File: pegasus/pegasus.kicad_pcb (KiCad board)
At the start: 2 copper layers, 50.8 x 126.4 mm, 10 parts, among them IC1 RFD900, IC2 Adafruit_MPL3115A2, IC3 Adafruit-BNO055-PCB, IC4 L70B-M39, IC5 L7805ACV, J1 Conn_01x02_Female, J2 Conn_01x02_Female, U1 Teensy4.1, U2 CON-SMA-EDGE-S, U3 CON-SMA-EDGE-S

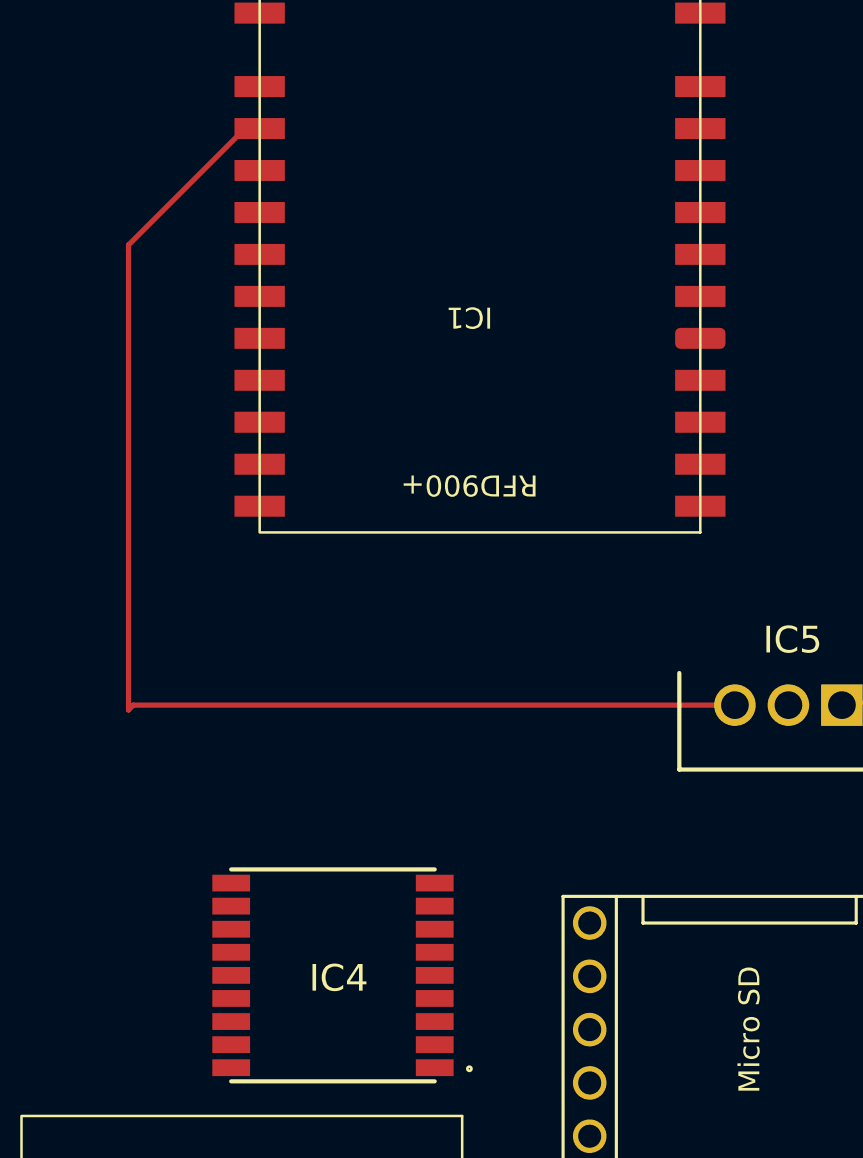
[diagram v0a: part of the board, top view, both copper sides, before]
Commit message: fixed UART wiring for gps and modem
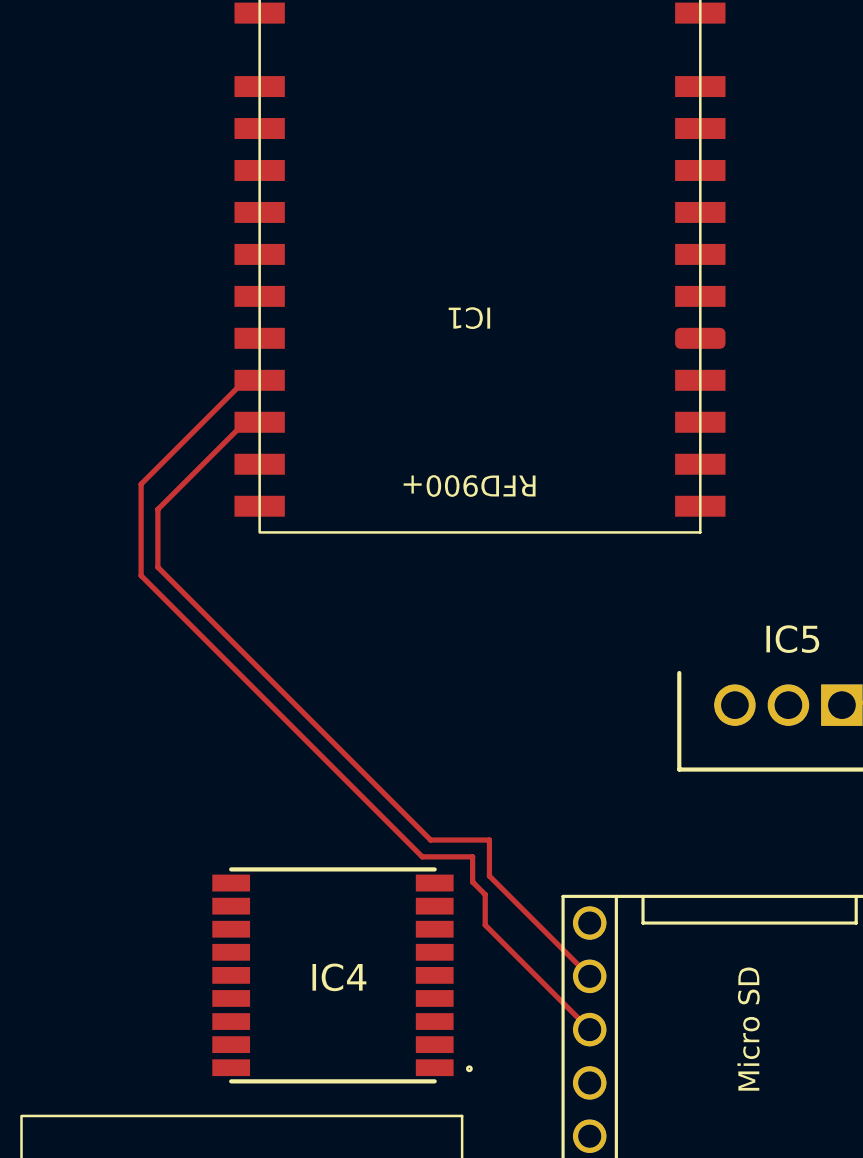
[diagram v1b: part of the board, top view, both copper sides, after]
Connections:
- net Net-(IC4-Pad2) renamed RX1
- net Net-(IC4-Pad3) renamed TX1
- U1 pad 26: Net-(IC1-Pad25) -> Net-(IC1-Pad26)
- U1 pad 27: Net-(IC1-Pad26) -> Net-(IC1-Pad25)
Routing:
- net /+5V: track 59.7 -> 0.70 mm
- net Net-(IC1-Pad25): track 0.00 -> 44.0 mm
- net Net-(IC1-Pad26): track 0.00 -> 39.0 mm

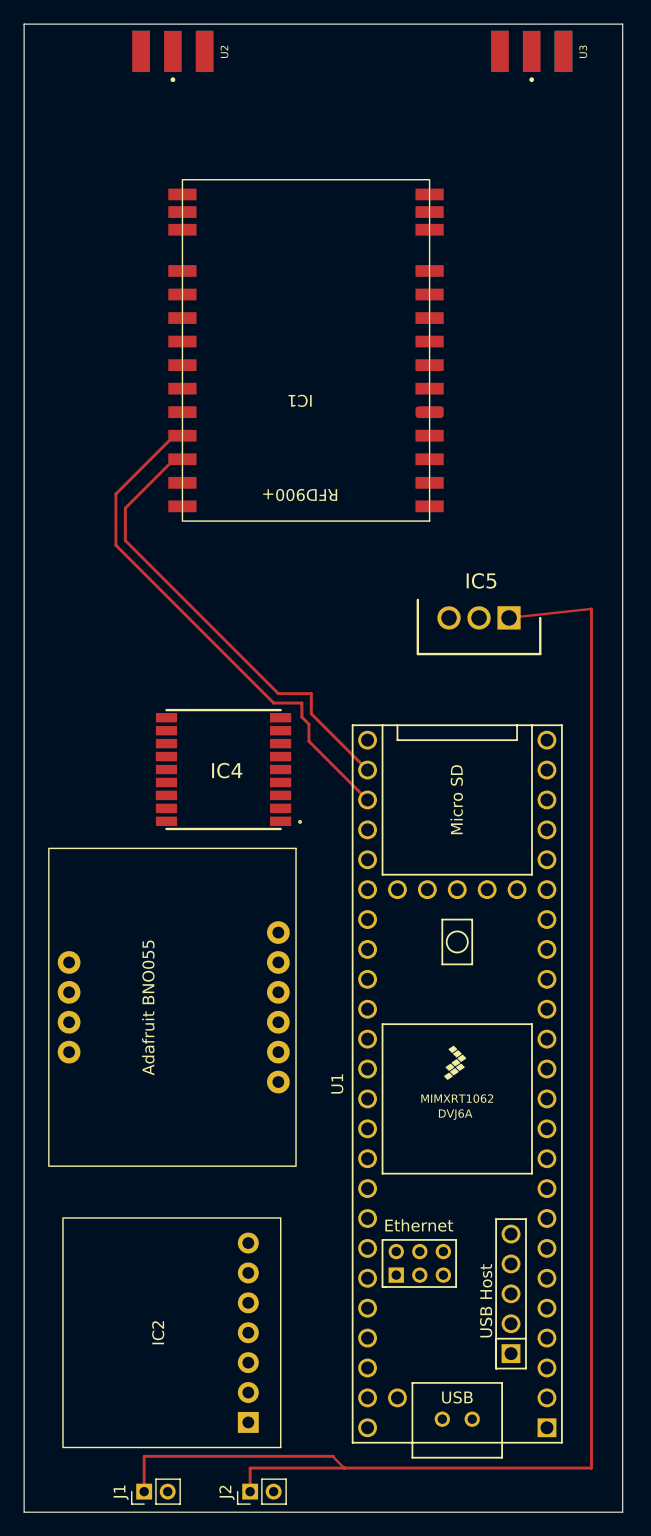
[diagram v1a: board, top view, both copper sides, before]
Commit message: finalized board dimensions (50x120mm) and component positioning. completed draft of traces
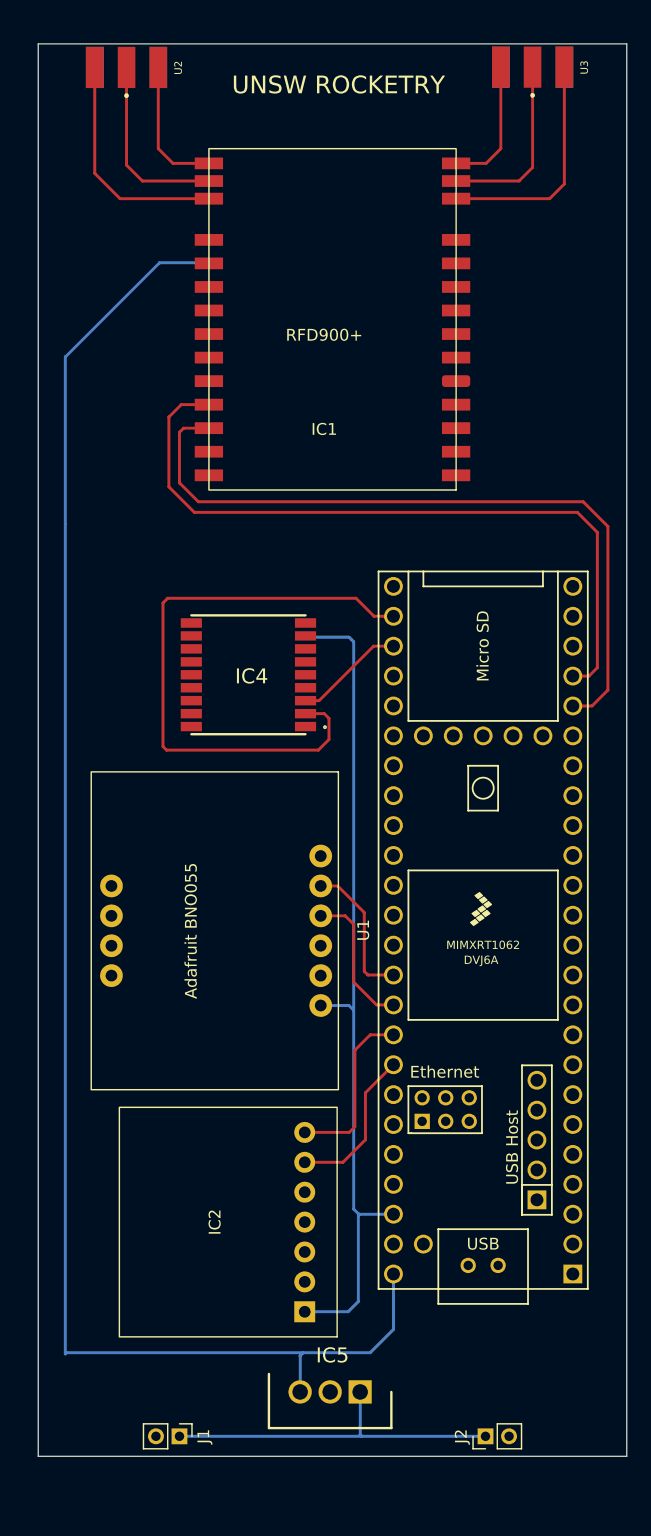
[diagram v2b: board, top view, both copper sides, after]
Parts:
- moved IC5 67.0 mm to (107.3, 154.5)
- moved J2 20.5 mm to (118.0, 158.3)
- moved U1 13.2 mm to (117.8, 115.3)
- moved IC2 10.6 mm to (100.1, 140.1)
- moved IC4 8.32 mm to (97.9, 93.6)
- moved IC3 7.43 mm to (104.0, 115.3)
- moved J1 5.58 mm to (92.0, 158.3), turned to -90 degrees
- moved U2 4.17 mm to (87.5, 42.0)
- moved IC1 3.47 mm to (109.5, 66.7)
- moved U3 1.33 mm to (122.0, 42.0)
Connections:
- net Net-(IC2-Pad1) renamed /+3.3V
- net Net-(IC2-Pad6) renamed /SCL
- net Net-(IC2-Pad7) renamed /SDA
- net Net-(IC3-Pad4)_1 renamed /SDA1
- net Net-(IC3-Pad5) renamed /SCL1
- IC1 pad 19: /+5V -> +5V
- IC1 pad 25: Net-(IC1-Pad25) -> TX7
- IC1 pad 26: Net-(IC1-Pad26) -> RX7
- IC4 pad 2: RX1 -> RX8
- IC4 pad 3: TX1 -> TX8
- IC5 pad 3: /+5V -> +5V
- U1 pad 2: TX1 -> unconnected-(U1-Pad2)
- U1 pad 20: unconnected-(U1-Pad20) -> RX7
- U1 pad 21: unconnected-(U1-Pad21) -> TX7
- U1 pad 26: Net-(IC1-Pad26) -> RX8
- U1 pad 27: Net-(IC1-Pad25) -> TX8
- U1 pad 3: RX1 -> unconnected-(U1-Pad3)
- U1 pad 48: 3.7V -> +5V
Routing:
- net +5V: track 0.00 -> 137.9 mm
- net 3.7V: track 123.2 -> 29.8 mm
- net /+3.3V: track 0.00 -> 71.3 mm
- net RX7: track 0.00 -> 62.3 mm
- net TX7: track 0.00 -> 61.6 mm
- net RX8: track 0.00 -> 51.1 mm
- net Net-(IC1-Pad25): track 44.0 -> 0.00 mm
- net Net-(IC1-Pad26): track 39.0 -> 0.00 mm
- net Net-(IC1-Pad12): track 0.00 -> 19.6 mm
- net Net-(IC1-Pad17): track 0.00 -> 19.6 mm
- net Net-(IC1-Pad16): track 0.00 -> 15.9 mm
- net Net-(IC1-Pad13): track 0.00 -> 15.5 mm
- net /SDA: track 0.00 -> 14.8 mm
- net /SCL: track 0.00 -> 13.3 mm
- net /SCL1: track 0.00 -> 12.2 mm
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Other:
- board size 50.8 x 126.4 mm -> 50 x 120 mm
- board text added: "UNSW ROCKETRY"

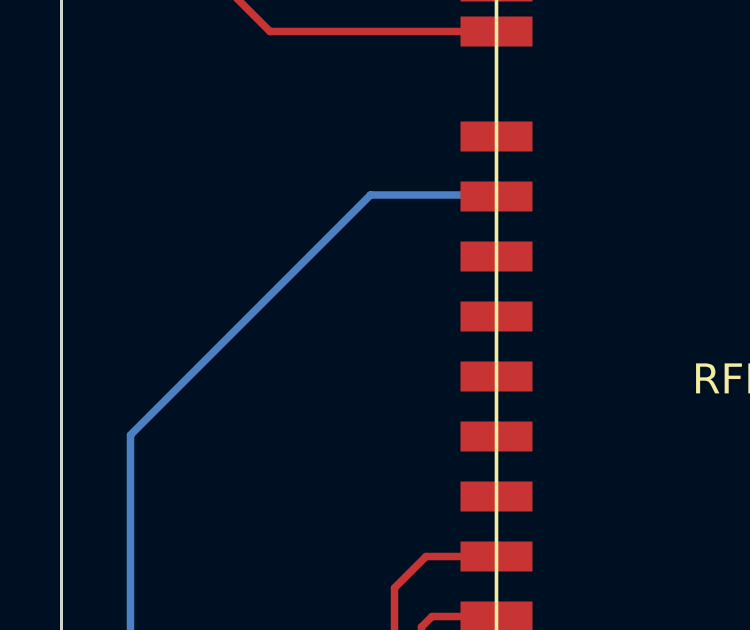
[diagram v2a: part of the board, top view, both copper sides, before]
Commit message: removed a wire
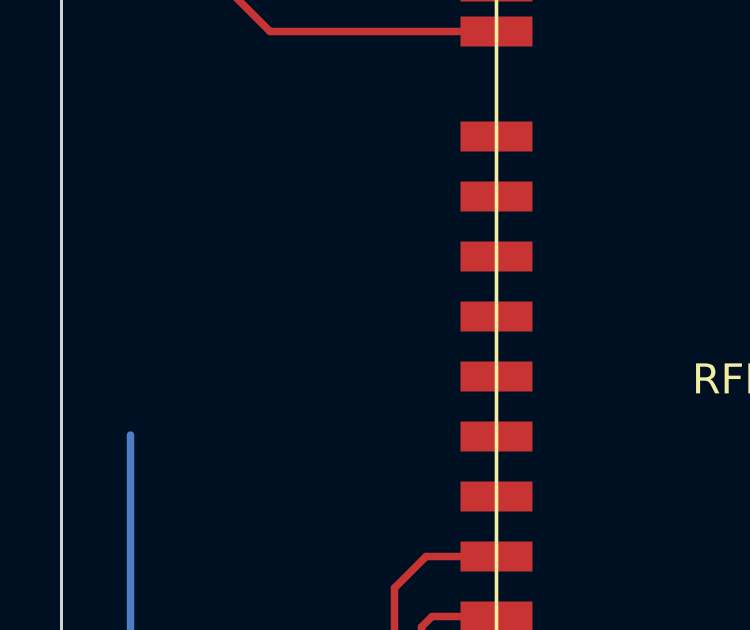
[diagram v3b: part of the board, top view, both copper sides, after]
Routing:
- net +5V: track 137.9 -> 123.3 mm
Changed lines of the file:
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@@
   (segment (start 104 111.54) (end 105.44 111.54) (width 0.25) (layer "F.Cu") (net 107))
   (segment (start 94.5 58.65) (end 93.8 58.65) (width 0.25) (layer "F.Cu") (net 108))
-  (segment (start 82.3 66.6) (end 90.3 58.6) (width 0.25) (layer "B.Cu") (net 108))
   (segment (start 82.3 80.8) (end 82.3 66.6) (width 0.25) (layer "B.Cu") (net 108))
   (segment (start 110.18 149.22) (end 110.18 144.51) (width 0.25) (layer "B.Cu") (net 108))
@@
   (segment (start 82.3 151.3) (end 82.3 80.8) (width 0.25) (layer "B.Cu") (net 108))
   (segment (start 108.2 151.2) (end 110.18 149.22) (width 0.25) (layer "B.Cu") (net 108))
-  (segment (start 90.3 58.6) (end 93.6 58.6) (width 0.25) (layer "B.Cu") (net 108))
   (segment (start 82.4 151.2) (end 82.3 151.3) (width 0.25) (layer "B.Cu") (net 108))
   (segment (start 102.5 151.2) (end 108.2 151.2) (width 0.25) (layer "B.Cu") (net 108))

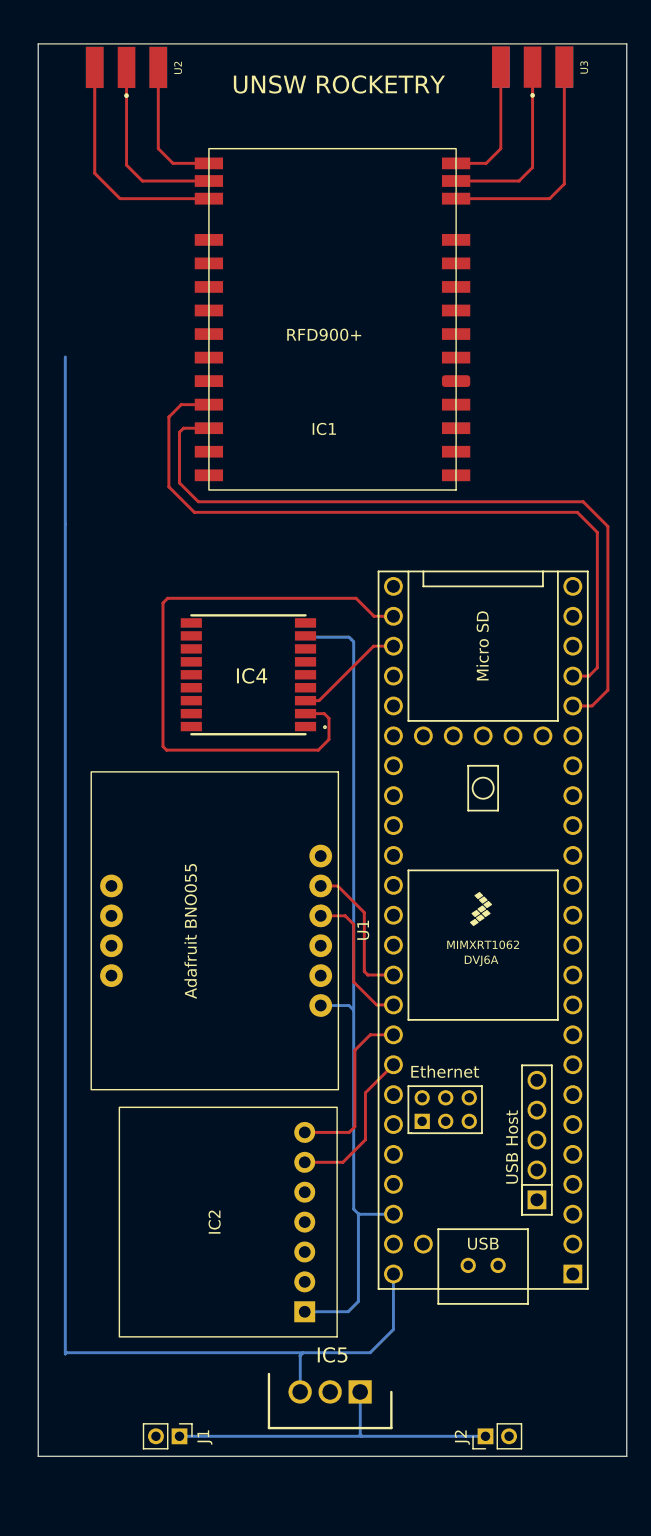
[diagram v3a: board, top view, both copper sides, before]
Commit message: added vias to trace power
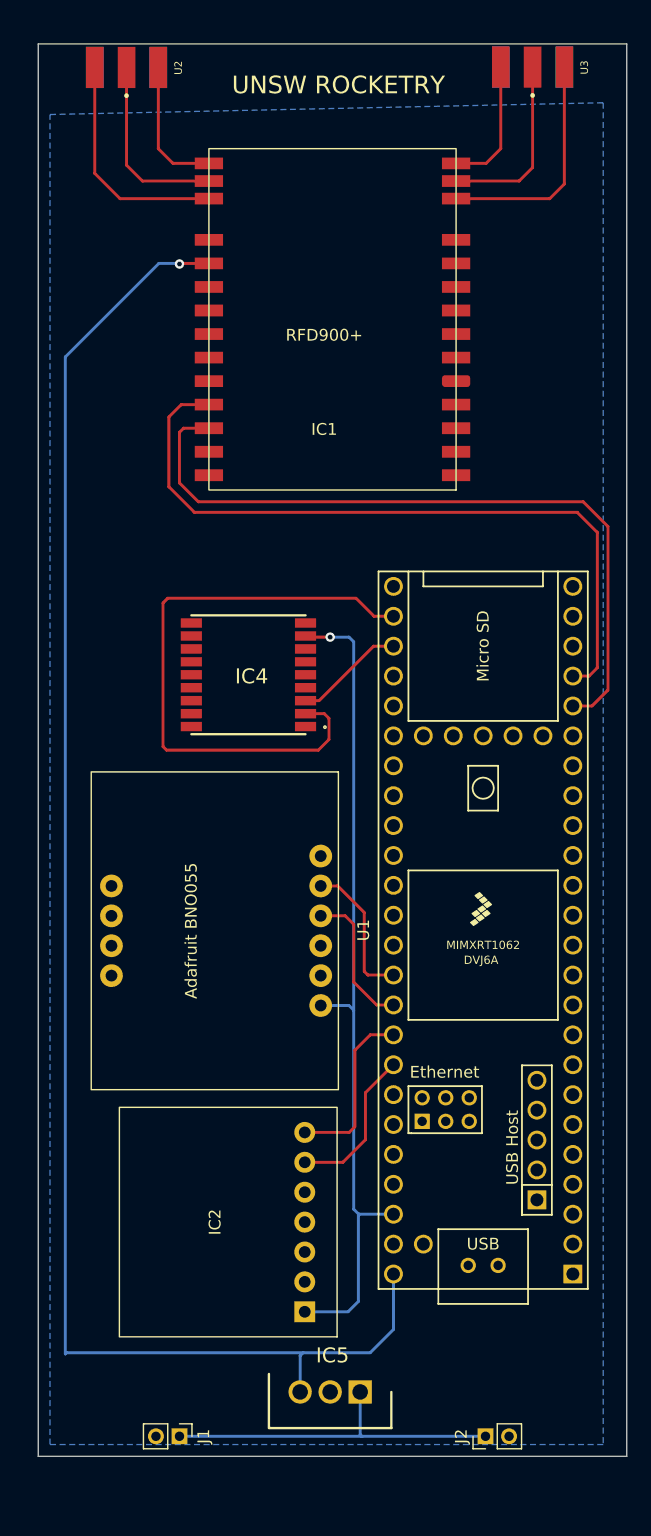
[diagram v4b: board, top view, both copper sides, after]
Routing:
- net +5V: track 123.3 -> 137.1 mm, vias 0 -> 1
- net /+3.3V: track 71.3 -> 71.4 mm, vias 0 -> 1
- added copper zone on B.Cu, net GND
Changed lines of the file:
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@@
   (segment (start 128.4 94.9) (end 128.4 81) (width 0.25) (layer "F.Cu") (net 102))
   (segment (start 92 77.3) (end 92 73) (width 0.25) (layer "F.Cu") (net 102))
+  (segment (start 102.807 90.4) (end 102.707 90.3) (width 0.25) (layer "F.Cu") (net 103))
+  (segment (start 104.8 90.4) (end 102.807 90.4) (width 0.25) (layer "F.Cu") (net 103))
+  (via (at 104.8 90.4) (size 0.8) (drill 0.4) (layers "F.Cu" "B.Cu") (net 103))
   (segment (start 106.32 147.72) (end 102.641 147.72) (width 0.25) (layer "B.Cu") (net 103))
   (segment (start 106.8 139) (end 106.8 122.1) (width 0.25) (layer "B.Cu") (net 103))
   (segment (start 107.25 139.45) (end 106.8 139) (width 0.25) (layer "B.Cu") (net 103))
-  (segment (start 106.4 90.4) (end 102.7 90.4) (width 0.25) (layer "B.Cu") (net 103))
-  (segment (start 106.6 90.6) (end 106.4 90.4) (width 0.25) (layer "B.Cu") (net 103))
+  (segment (start 106.4 90.4) (end 106.8 90.8) (width 0.25) (layer "B.Cu") (net 103))
   (segment (start 107.2 146.84) (end 106.32 147.72) (width 0.25) (layer "B.Cu") (net 103))
   (segment (start 110.18 139.43) (end 107.27 139.43) (width 0.25) (layer "B.Cu") (net 103))
+  (segment (start 106.8 90.8) (end 106.8 122.1) (width 0.25) (layer "B.Cu") (net 103))
   (segment (start 107.27 139.43) (end 107.25 139.45) (width 0.25) (layer "B.Cu") (net 103))
   (segment (start 106.8 122.1) (end 106.4 121.7) (width 0.25) (layer "B.Cu") (net 103))
-  (segment (start 106.8 90.8) (end 106.6 90.6) (width 0.25) (layer "B.Cu") (net 103))
-  (segment (start 106.8 122.1) (end 106.8 90.8) (width 0.25) (layer "B.Cu") (net 103))
+  (segment (start 106.4 90.4) (end 104.8 90.4) (width 0.25) (layer "B.Cu") (net 103))
   (segment (start 107.2 139.5) (end 107.2 146.84) (width 0.25) (layer "B.Cu") (net 103))
   (segment (start 107.25 139.45) (end 107.2 139.5) (width 0.25) (layer "B.Cu") (net 103))
@@
   (segment (start 107.7 113.8) (end 107.7 118.8) (width 0.25) (layer "F.Cu") (net 107))
   (segment (start 104 111.54) (end 105.44 111.54) (width 0.25) (layer "F.Cu") (net 107))
-  (segment (start 94.5 58.65) (end 93.8 58.65) (width 0.25) (layer "F.Cu") (net 108))
-  (segment (start 82.3 80.8) (end 82.3 66.6) (width 0.25) (layer "B.Cu") (net 108))
+  (segment (start 92 58.6) (end 92.05 58.65) (width 0.25) (layer "F.Cu") (net 108))
+  (segment (start 92.05 58.65) (end 94.5 58.65) (width 0.25) (layer "F.Cu") (net 108))
+  (via (at 92 58.7) (size 0.8) (drill 0.4) (layers "F.Cu" "B.Cu") (net 108))
+  (segment (start 102.5 151.2) (end 82.4 151.2) (width 0.25) (layer "B.Cu") (net 108))
   (segment (start 110.18 149.22) (end 110.18 144.51) (width 0.25) (layer "B.Cu") (net 108))
+  (segment (start 91.95 58.65) (end 92 58.7) (width 0.25) (layer "B.Cu") (net 108))
   (segment (start 102.25 151.45) (end 102.5 151.2) (width 0.25) (layer "B.Cu") (net 108))
+  (segment (start 82.3 151.3) (end 82.3 66.6) (width 0.25) (layer "B.Cu") (net 108))
+  (segment (start 90.25 58.65) (end 91.95 58.65) (width 0.25) (layer "B.Cu") (net 108))
   (segment (start 102.25 154.53) (end 102.25 151.45) (width 0.25) (layer "B.Cu") (net 108))
-  (segment (start 93.6 58.6) (end 94.6 58.6) (width 0.25) (layer "B.Cu") (net 108))
-  (segment (start 102.5 151.2) (end 82.4 151.2) (width 0.25) (layer "B.Cu") (net 108))
-  (segment (start 82.3 151.3) (end 82.3 80.8) (width 0.25) (layer "B.Cu") (net 108))
   (segment (start 108.2 151.2) (end 110.18 149.22) (width 0.25) (layer "B.Cu") (net 108))
   (segment (start 82.4 151.2) (end 82.3 151.3) (width 0.25) (layer "B.Cu") (net 108))
   (segment (start 102.5 151.2) (end 108.2 151.2) (width 0.25) (layer "B.Cu") (net 108))
+  (segment (start 82.3 66.6) (end 90.25 58.65) (width 0.25) (layer "B.Cu") (net 108))
+  (zone (net 2) (net_name "GND") (layer "B.Cu") (hatch edge 0.508)
+    (connect_pads (clearance 0.508))
+    (min_thickness 0.254)
+    (fill (thermal_gap 0.508) (thermal_bridge_width 0.508))
+    (polygon
+      (pts
+        (xy 128 159)
+        (xy 81 159)
+        (xy 81 46)
+        (xy 128 45)
+      )
+    )
+  )
 )
